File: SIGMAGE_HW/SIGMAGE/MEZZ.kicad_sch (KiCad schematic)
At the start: 4 parts, among them J12 DF40C-40DS-0.4V_51, J13 DF40C-40DP-0.4V_51, J14 DF40C-40DS-0.4V_51, J8 DF40C-40DP-0.4V_51

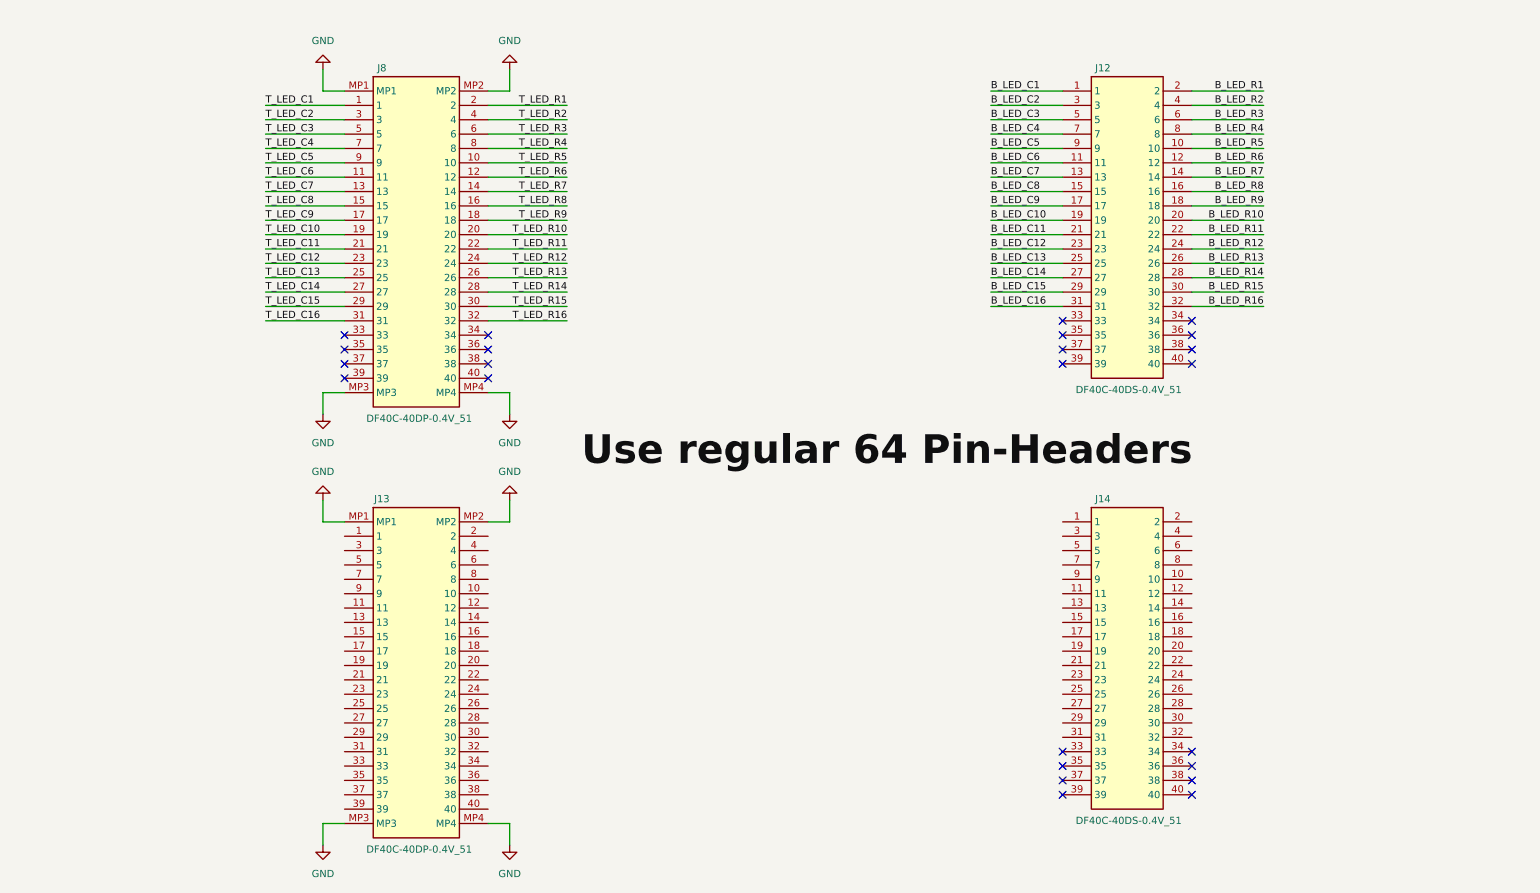
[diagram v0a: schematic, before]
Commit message: added board interconnect headers
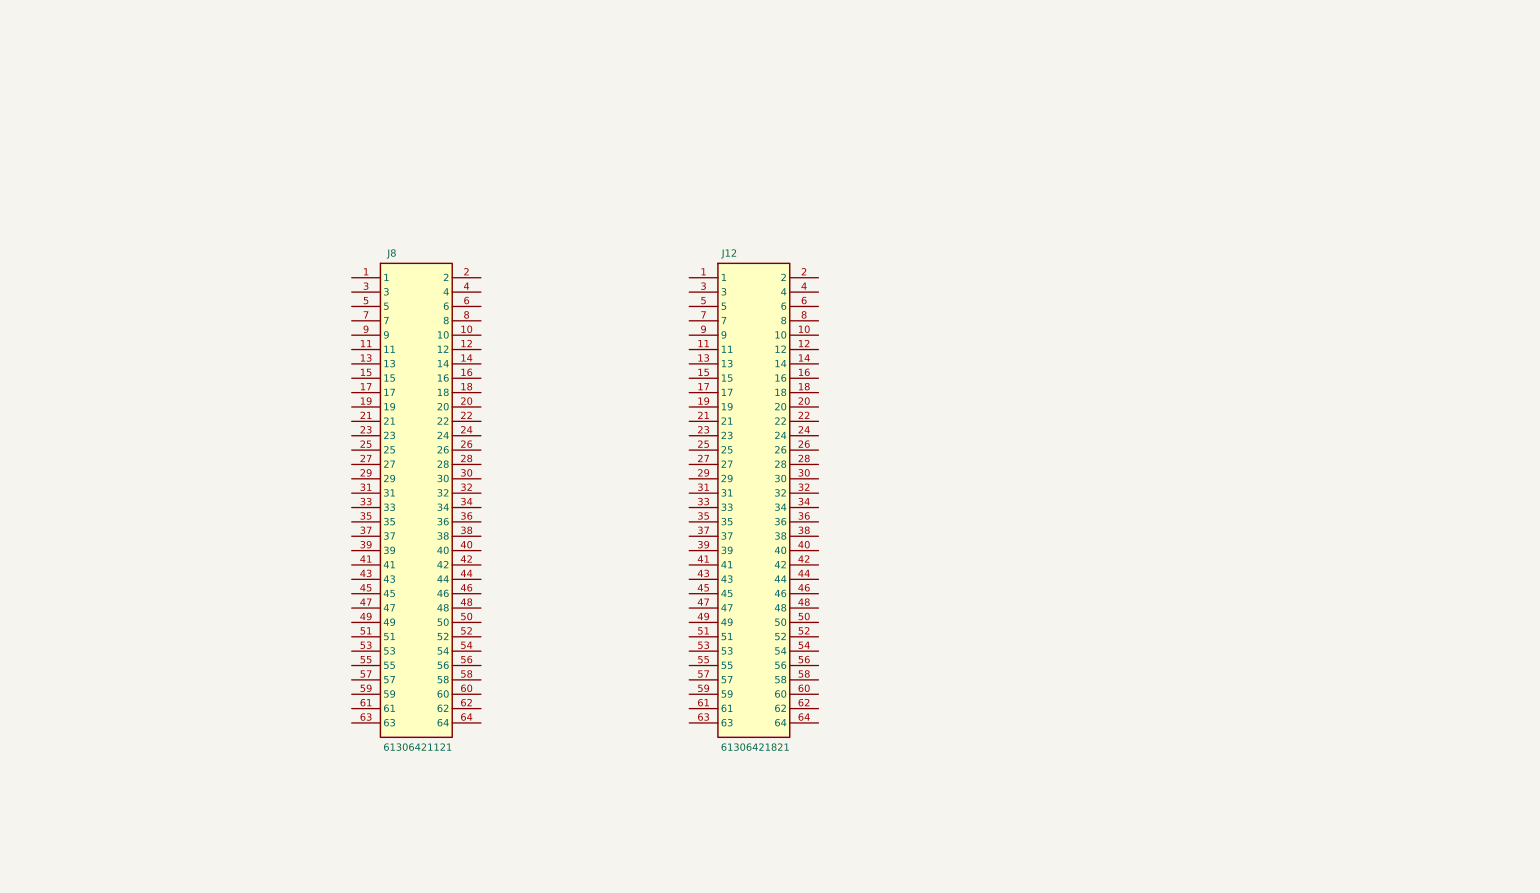
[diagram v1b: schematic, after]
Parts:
- removed J12, J14: DF40C-40DS-0.4V_51, SIGMAGE:DF40C40DS04V51, symbol SIGMAGE:DF40C40DS04V51
- removed J13, J8: DF40C-40DP-0.4V_51, SIGMAGE:DF40C40DP04V51, symbol SIGMAGE:DF40C40DP04V51
- added J12: 61306421821, SIGMAGE:61306421821, symbol SIGMAGE:61306421821
- added J8: 61306421121, SIGMAGE:61306421121, symbol SIGMAGE:61306421121
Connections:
- no-connect marks 24 -> 0

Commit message: finished schematic
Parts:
- added J13: 61306421121, SIGMAGE:61306421121, symbol SIGMAGE:61306421121
- added J14: 61306421821, SIGMAGE:61306421821, symbol SIGMAGE:61306421821
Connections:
- net 1_RE1_A: now reaches J12.1
- net 1_RE11_B: now reaches J12.10
- net 1_RE2_C: now reaches J12.11
- net 1_RE11_C: now reaches J12.12
- net 1_RE3_A: now reaches J12.13
- net 1_RE12_A: now reaches J12.14
- net 1_RE3_B: now reaches J12.15
- net 1_RE12_B: now reaches J12.16
- net 1_RE3_C: now reaches J12.17
- net 1_RE12_C: now reaches J12.18
- net 1_RE4_A: now reaches J12.19
- net 1_RE10_A: now reaches J12.2
- net 1_RE13_A: now reaches J12.20
- net 1_RE4_B: now reaches J12.21
- net 1_RE13_B: now reaches J12.22
- net 1_RE4_C: now reaches J12.23
- net 1_RE13_C: now reaches J12.24
- net 1_RE5_A: now reaches J12.25
- net 1_RE14_A: now reaches J12.26
- net 1_RE5_B: now reaches J12.27
- net 1_RE14_B: now reaches J12.28
- net 1_RE5_C: now reaches J12.29
- net 1_RE1_B: now reaches J12.3
- net 1_RE14_C: now reaches J12.30
- net 1_RE6_A: now reaches J12.31
- net 1_RE15_A: now reaches J12.32
- net 1_RE6_B: now reaches J12.33
- net 1_RE15_B: now reaches J12.34
- net 1_RE6_C: now reaches J12.35
- net 1_RE15_C: now reaches J12.36
- net 1_RE7_A: now reaches J12.37
- net 1_RE16_A: now reaches J12.38
- net 1_RE7_B: now reaches J12.39
- net 1_RE10_B: now reaches J12.4
- net 1_RE16_B: now reaches J12.40
- net 1_RE7_C: now reaches J12.41
- net 1_RE16_C: now reaches J12.42
- net 1_RE8_A: now reaches J12.43
- net 1_RE17_A: now reaches J12.44
- net 1_RE8_B: now reaches J12.45
- net 1_RE17_B: now reaches J12.46
- net 1_RE8_C: now reaches J12.47
- net 1_RE17_C: now reaches J12.48
- net 1_RE9_A: now reaches J12.49
- net 1_RE1_C: now reaches J12.5
- net 1_RE18_A: now reaches J12.50
- net 1_RE9_B: now reaches J12.51
- net 1_RE18_B: now reaches J12.52
- net 1_RE9_C: now reaches J12.53
- net 1_RE18_C: now reaches J12.54
- net 1_RE10_C: now reaches J12.6
- net 1_RE2_A: now reaches J12.7
- net 1_RE11_A: now reaches J12.8
- net 1_RE2_B: now reaches J12.9
- net 0_RE1_A: now reaches J8.1
- net 0_RE11_B: now reaches J8.10
- net 0_RE2_C: now reaches J8.11
- net 0_RE11_C: now reaches J8.12
- net 0_RE3_A: now reaches J8.13
- net 0_RE12_A: now reaches J8.14
- net 0_RE3_B: now reaches J8.15
- net 0_RE12_B: now reaches J8.16
- net 0_RE3_C: now reaches J8.17
- net 0_RE12_C: now reaches J8.18
- net 0_RE4_A: now reaches J8.19
- net 0_RE10_A: now reaches J8.2
- net 0_RE13_A: now reaches J8.20
- net 0_RE4_B: now reaches J8.21
- net 0_RE13_B: now reaches J8.22
- net 0_RE4_C: now reaches J8.23
- net 0_RE13_C: now reaches J8.24
- net 0_RE5_A: now reaches J8.25
- net 0_RE14_A: now reaches J8.26
- net 0_RE5_B: now reaches J8.27
- net 0_RE14_B: now reaches J8.28
- net 0_RE5_C: now reaches J8.29
- net 0_RE1_B: now reaches J8.3
- net 0_RE14_C: now reaches J8.30
- net 0_RE6_A: now reaches J8.31
- net 0_RE15_A: now reaches J8.32
- net 0_RE6_B: now reaches J8.33
- net 0_RE15_B: now reaches J8.34
- net 0_RE6_C: now reaches J8.35
- net 0_RE15_C: now reaches J8.36
- net 0_RE7_A: now reaches J8.37
- net 0_RE16_A: now reaches J8.38
- net 0_RE7_B: now reaches J8.39
- net 0_RE10_B: now reaches J8.4
- net 0_RE16_B: now reaches J8.40
- net 0_RE7_C: now reaches J8.41
- net 0_RE16_C: now reaches J8.42
- net 0_RE8_A: now reaches J8.43
- net 0_RE17_A: now reaches J8.44
- net 0_RE8_B: now reaches J8.45
- net 0_RE17_B: now reaches J8.46
- net 0_RE8_C: now reaches J8.47
- net 0_RE17_C: now reaches J8.48
- net 0_RE9_A: now reaches J8.49
- net 0_RE1_C: now reaches J8.5
- net 0_RE18_A: now reaches J8.50
- net 0_RE9_B: now reaches J8.51
- net 0_RE18_B: now reaches J8.52
- net 0_RE9_C: now reaches J8.53
- net 0_RE18_C: now reaches J8.54
- net 0_RE10_C: now reaches J8.6
- net 0_RE2_A: now reaches J8.7
- net 0_RE11_A: now reaches J8.8
- net 0_RE2_B: now reaches J8.9
- new net 0_LED_C1: J13.1
- new net 0_LED_C10: J13.19
- new net 0_LED_C11: J13.21
- new net 0_LED_C12: J13.23
- new net 0_LED_C13: J13.25
- new net 0_LED_C14: J13.27
- new net 0_LED_C15: J13.29
- new net 0_LED_C16: J13.31
- new net 0_LED_C2: J13.3
- new net 0_LED_C3: J13.5
- new net 0_LED_C4: J13.7
- new net 0_LED_C5: J13.9
- new net 0_LED_C6: J13.11
- new net 0_LED_C7: J13.13
- new net 0_LED_C8: J13.15
- new net 0_LED_C9: J13.17
- new net 0_LED_R1: J13.2
- new net 0_LED_R10: J13.20
- new net 0_LED_R11: J13.22
- new net 0_LED_R12: J13.24
- new net 0_LED_R13: J13.26
- new net 0_LED_R14: J13.28
- new net 0_LED_R15: J13.30
- new net 0_LED_R16: J13.32
- new net 0_LED_R2: J13.4
- new net 0_LED_R3: J13.6
- new net 0_LED_R4: J13.8
- new net 0_LED_R5: J13.10
- new net 0_LED_R6: J13.12
- new net 0_LED_R7: J13.14
- new net 0_LED_R8: J13.16
- new net 0_LED_R9: J13.18
- new net 0_SW1: J13.37
- new net 0_SW10: J13.55
- new net 0_SW11: J13.57
- new net 0_SW12: J13.59
- new net 0_SW2: J13.39
- new net 0_SW3: J13.41
- new net 0_SW4: J13.43
- new net 0_SW5: J13.45
- new net 0_SW6: J13.47
- new net 0_SW7: J13.49
- new net 0_SW8: J13.51
- new net 0_SW9: J13.53
- new net 1_LED_C1: J14.1
- new net 1_LED_C10: J14.19
- new net 1_LED_C11: J14.21
- new net 1_LED_C12: J14.23
- new net 1_LED_C13: J14.25
- new net 1_LED_C14: J14.27
- new net 1_LED_C15: J14.29
- new net 1_LED_C16: J14.31
- new net 1_LED_C2: J14.3
- new net 1_LED_C3: J14.5
- new net 1_LED_C4: J14.7
- new net 1_LED_C5: J14.9
- new net 1_LED_C6: J14.11
- new net 1_LED_C7: J14.13
- new net 1_LED_C8: J14.15
- new net 1_LED_C9: J14.17
- new net 1_LED_R1: J14.2
- new net 1_LED_R10: J14.20
- new net 1_LED_R11: J14.22
- new net 1_LED_R12: J14.24
- new net 1_LED_R13: J14.26
- new net 1_LED_R14: J14.28
- new net 1_LED_R15: J14.30
- new net 1_LED_R16: J14.32
- new net 1_LED_R2: J14.4
- new net 1_LED_R3: J14.6
- new net 1_LED_R4: J14.8
- new net 1_LED_R5: J14.10
- new net 1_LED_R6: J14.12
- new net 1_LED_R7: J14.14
- new net 1_LED_R8: J14.16
- new net 1_LED_R9: J14.18
- new net 1_SW1: J14.37
- new net 1_SW10: J14.55
- new net 1_SW11: J14.57
- new net 1_SW12: J14.59
- new net 1_SW2: J14.39
- new net 1_SW3: J14.41
- new net 1_SW4: J14.43
- new net 1_SW5: J14.45
- new net 1_SW6: J14.47
- new net 1_SW7: J14.49
- new net 1_SW8: J14.51
- new net 1_SW9: J14.53
- no-connect marks 0 -> 60
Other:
- moved on the sheet: J12, J8

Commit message: basic layout
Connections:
- net 0_LED_C1: no longer J13.1
- net 0_LED_C10: no longer J13.19
- net 0_LED_C11: no longer J13.21
- net 0_LED_C12: no longer J13.23
- net 0_LED_C13: no longer J13.25
- net 0_LED_C14: no longer J13.27
- net 0_LED_C15: no longer J13.29
- net 0_LED_C16: no longer J13.31
- net 0_LED_C2: no longer J13.3
- net 0_LED_C3: no longer J13.5
- net 0_LED_C4: no longer J13.7
- net 0_LED_C5: no longer J13.9
- net 0_LED_C6: no longer J13.11
- net 0_LED_C7: no longer J13.13
- net 0_LED_C8: no longer J13.15
- net 0_LED_C9: no longer J13.17
- net 0_LED_R1: no longer J13.2
- net 0_LED_R10: no longer J13.20
- net 0_LED_R11: no longer J13.22
- net 0_LED_R12: no longer J13.24
- net 0_LED_R13: no longer J13.26
- net 0_LED_R14: no longer J13.28
- net 0_LED_R15: no longer J13.30
- net 0_LED_R16: no longer J13.32
- net 0_LED_R2: no longer J13.4
- net 0_LED_R3: no longer J13.6
- net 0_LED_R4: no longer J13.8
- net 0_LED_R5: no longer J13.10
- net 0_LED_R6: no longer J13.12
- net 0_LED_R7: no longer J13.14
- net 0_LED_R8: no longer J13.16
- net 0_LED_R9: no longer J13.18
- net 0_RE10_A: no longer J8.2
- net 0_RE10_B: no longer J8.4
- net 0_RE10_C: no longer J8.6
- net 0_RE11_A: no longer J8.8
- net 0_RE11_B: no longer J8.10
- net 0_RE11_C: no longer J8.12
- net 0_RE12_A: no longer J8.14
- net 0_RE12_B: no longer J8.16
- net 0_RE12_C: no longer J8.18
- net 0_RE13_A: no longer J8.20
- net 0_RE13_B: no longer J8.22
- net 0_RE13_C: no longer J8.24
- net 0_RE14_A: no longer J8.26
- net 0_RE14_B: no longer J8.28
- net 0_RE14_C: no longer J8.30
- net 0_RE15_A: no longer J8.32
- net 0_RE15_B: no longer J8.34
- net 0_RE15_C: no longer J8.36
- net 0_RE16_A: no longer J8.38
- net 0_RE16_B: no longer J8.40
- net 0_RE16_C: no longer J8.42
- net 0_RE17_A: no longer J8.44
- net 0_RE17_B: no longer J8.46
- net 0_RE17_C: no longer J8.48
- net 0_RE18_A: no longer J8.50
- net 0_RE18_B: no longer J8.52
- net 0_RE18_C: no longer J8.54
- net 0_RE1_A: no longer J8.1
- net 0_RE1_B: no longer J8.3
- net 0_RE1_C: no longer J8.5
- net 0_RE2_A: no longer J8.7
- net 0_RE2_B: no longer J8.9
- net 0_RE2_C: no longer J8.11
- net 0_RE3_A: no longer J8.13
- net 0_RE3_B: no longer J8.15
- net 0_RE3_C: no longer J8.17
- net 0_RE4_A: no longer J8.19
- net 0_RE4_B: no longer J8.21
- net 0_RE4_C: no longer J8.23
- net 0_RE5_A: no longer J8.25
- net 0_RE5_B: no longer J8.27
- net 0_RE5_C: no longer J8.29
- net 0_RE6_A: no longer J8.31
- net 0_RE6_B: no longer J8.33
- net 0_RE6_C: no longer J8.35
- net 0_RE7_A: no longer J8.37
- net 0_RE7_B: no longer J8.39
- net 0_RE7_C: no longer J8.41
- net 0_RE8_A: no longer J8.43
- net 0_RE8_B: no longer J8.45
- net 0_RE8_C: no longer J8.47
- net 0_RE9_A: no longer J8.49
- net 0_RE9_B: no longer J8.51
- net 0_RE9_C: no longer J8.53
- net 0_SW1: no longer J13.37
- net 0_SW10: no longer J13.55
- net 0_SW11: no longer J13.57
- net 0_SW12: no longer J13.59
- net 0_SW2: no longer J13.39
- net 0_SW3: no longer J13.41
- net 0_SW4: no longer J13.43
- net 0_SW5: no longer J13.45
- net 0_SW6: no longer J13.47
- net 0_SW7: no longer J13.49
- net 0_SW8: no longer J13.51
- net 0_SW9: no longer J13.53
- net 1_LED_C1: no longer J14.1
- net 1_LED_C10: no longer J14.19
- net 1_LED_C11: no longer J14.21
- net 1_LED_C12: no longer J14.23
- net 1_LED_C13: no longer J14.25
- net 1_LED_C14: no longer J14.27
- net 1_LED_C15: no longer J14.29
- net 1_LED_C16: no longer J14.31
- net 1_LED_C2: no longer J14.3
- net 1_LED_C3: no longer J14.5
- net 1_LED_C4: no longer J14.7
- net 1_LED_C5: no longer J14.9
- net 1_LED_C6: no longer J14.11
- net 1_LED_C7: no longer J14.13
- net 1_LED_C8: no longer J14.15
- net 1_LED_C9: no longer J14.17
- net 1_LED_R1: no longer J14.2
- net 1_LED_R10: no longer J14.20
- net 1_LED_R11: no longer J14.22
- net 1_LED_R12: no longer J14.24
- net 1_LED_R13: no longer J14.26
- net 1_LED_R14: no longer J14.28
- net 1_LED_R15: no longer J14.30
- net 1_LED_R16: no longer J14.32
- net 1_LED_R2: no longer J14.4
- net 1_LED_R3: no longer J14.6
- net 1_LED_R4: no longer J14.8
- net 1_LED_R5: no longer J14.10
- net 1_LED_R6: no longer J14.12
- net 1_LED_R7: no longer J14.14
- net 1_LED_R8: no longer J14.16
- net 1_LED_R9: no longer J14.18
- net 1_RE10_A: no longer J12.2
- net 1_RE10_B: no longer J12.4
- net 1_RE10_C: no longer J12.6
- net 1_RE11_A: no longer J12.8
- net 1_RE11_B: no longer J12.10
- net 1_RE11_C: no longer J12.12
- net 1_RE12_A: no longer J12.14
- net 1_RE12_B: no longer J12.16
- net 1_RE12_C: no longer J12.18
- net 1_RE13_A: no longer J12.20
- net 1_RE13_B: no longer J12.22
- net 1_RE13_C: no longer J12.24
- net 1_RE14_A: no longer J12.26
- net 1_RE14_B: no longer J12.28
- net 1_RE14_C: no longer J12.30
- net 1_RE15_A: no longer J12.32
- net 1_RE15_B: no longer J12.34
- net 1_RE15_C: no longer J12.36
- net 1_RE16_A: no longer J12.38
- net 1_RE16_B: no longer J12.40
- net 1_RE16_C: no longer J12.42
- net 1_RE17_A: no longer J12.44
- net 1_RE17_B: no longer J12.46
- net 1_RE17_C: no longer J12.48
- net 1_RE18_A: no longer J12.50
- net 1_RE18_B: no longer J12.52
- net 1_RE18_C: no longer J12.54
- net 1_RE1_A: no longer J12.1
- net 1_RE1_B: no longer J12.3
- net 1_RE1_C: no longer J12.5
- net 1_RE2_A: no longer J12.7
- net 1_RE2_B: no longer J12.9
- net 1_RE2_C: no longer J12.11
- net 1_RE3_A: no longer J12.13
- net 1_RE3_B: no longer J12.15
- net 1_RE3_C: no longer J12.17
- net 1_RE4_A: no longer J12.19
- net 1_RE4_B: no longer J12.21
- net 1_RE4_C: no longer J12.23
- net 1_RE5_A: no longer J12.25
- net 1_RE5_B: no longer J12.27
- net 1_RE5_C: no longer J12.29
- net 1_RE6_A: no longer J12.31
- net 1_RE6_B: no longer J12.33
- net 1_RE6_C: no longer J12.35
- net 1_RE7_A: no longer J12.37
- net 1_RE7_B: no longer J12.39
- net 1_RE7_C: no longer J12.41
- net 1_RE8_A: no longer J12.43
- net 1_RE8_B: no longer J12.45
- net 1_RE8_C: no longer J12.47
- net 1_RE9_A: no longer J12.49
- net 1_RE9_B: no longer J12.51
- net 1_RE9_C: no longer J12.53
- net 1_SW1: no longer J14.37
- net 1_SW10: no longer J14.55
- net 1_SW11: no longer J14.57
- net 1_SW12: no longer J14.59
- net 1_SW2: no longer J14.39
- net 1_SW3: no longer J14.41
- net 1_SW4: no longer J14.43
- net 1_SW5: no longer J14.45
- net 1_SW6: no longer J14.47
- net 1_SW7: no longer J14.49
- net 1_SW8: no longer J14.51
- net 1_SW9: no longer J14.53

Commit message: uga uga
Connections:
- net 1_LED_C1: now also J14.47
- net 1_LED_C10: now also J14.40
- net 1_LED_C11: now also J14.37
- net 1_LED_C12: now also J14.38
- net 1_LED_C13: now also J14.35
- net 1_LED_C14: now also J14.36
- net 1_LED_C15: now also J14.33
- net 1_LED_C16: now also J14.34
- net 1_LED_C2: now also J14.48
- net 1_LED_C3: now also J14.45
- net 1_LED_C4: now also J14.46
- net 1_LED_C5: now also J14.43
- net 1_LED_C6: now also J14.44
- net 1_LED_C7: now also J14.41
- net 1_LED_C8: now also J14.42
- net 1_LED_C9: now also J14.39
- net 1_LED_R1: now also J14.63
- net 1_LED_R10: now also J14.56
- net 1_LED_R11: now also J14.53
- net 1_LED_R12: now also J14.54
- net 1_LED_R13: now also J14.51
- net 1_LED_R14: now also J14.52
- net 1_LED_R15: now also J14.49
- net 1_LED_R16: now also J14.50
- net 1_LED_R2: now also J14.64
- net 1_LED_R3: now also J14.61
- net 1_LED_R4: now also J14.62
- net 1_LED_R5: now also J14.59
- net 1_LED_R6: now also J14.60
- net 1_LED_R7: now also J14.57
- net 1_LED_R8: now also J14.58
- net 1_LED_R9: now also J14.55
- net 1_RE10_A: now also J12.48
- net 1_RE10_B: now also J12.47
- net 1_RE10_C: now also J12.49
- net 1_RE11_A: now also J12.15
- net 1_RE11_B: now also J12.13
- net 1_RE11_C: now also J12.17
- net 1_RE12_A: now also J12.9
- net 1_RE12_B: now also J12.7
- net 1_RE12_C: now also J12.11
- net 1_RE13_A: now also J14.31
- net 1_RE13_B: now also J14.32
- net 1_RE13_C: now also J14.29
- net 1_RE14_A: now also J14.30
- net 1_RE14_B: now also J14.27
- net 1_RE14_C: now also J14.28
- net 1_RE15_A: now also J14.25
- net 1_RE15_B: now also J14.24
- net 1_RE15_C: now also J14.26
- net 1_RE1_A: now also J12.61
- net 1_RE1_B: now also J12.59
- net 1_RE1_C: now also J12.63
- net 1_RE2_A: now also J12.57
- net 1_RE2_B: now also J12.56
- net 1_RE2_C: now also J12.58
- net 1_RE3_A: now also J12.54
- net 1_RE3_B: now also J12.53
- net 1_RE3_C: now also J12.55
- net 1_RE4_A: now also J12.51
- net 1_RE4_B: now also J12.50
- net 1_RE4_C: now also J12.52
- net 1_RE5_A: now also J12.3
- net 1_RE5_B: now also J12.1
- net 1_RE5_C: now also J12.5
- net 1_RE6_A: now also J14.22
- net 1_RE6_B: now also J14.21
- net 1_RE6_C: now also J14.23
- net 1_RE7_A: now also J14.19
- net 1_RE7_B: now also J14.18
- net 1_RE7_C: now also J14.20
- net 1_RE8_A: now also J14.16
- net 1_RE8_B: now also J14.15
- net 1_RE8_C: now also J14.17
- net 1_RE9_A: now also J12.64
- net 1_RE9_B: now also J12.60
- net 1_RE9_C: now also J12.62
- net 1_SW1: now also J12.45
- net 1_SW2: now also J12.43
- net 1_SW3: now also J12.41
- net 1_SW4: now also J12.39
- net 1_SW5: now also J12.37
- net 1_LED11: now reaches J12.10
- net 1_LED10: now reaches J12.12
- net 1_LED9: now reaches J12.14
- net 1_LED8: now reaches J12.16
- net 1_LED7: now reaches J12.18
- net 1_LED15: now reaches J12.2
- net 1_LED6: now reaches J12.20
- net 1_LED5: now reaches J12.36
- net 1_LED4: now reaches J12.38
- net 1_LED14: now reaches J12.4
- net 1_LED3: now reaches J12.40
- net 1_LED2: now reaches J12.42
- net 1_LED1: now reaches J12.44
- net 1_LED0: now reaches J12.46
- net 1_LED13: now reaches J12.6
- net 1_LED12: now reaches J12.8
- no-connect marks 60 -> 2
